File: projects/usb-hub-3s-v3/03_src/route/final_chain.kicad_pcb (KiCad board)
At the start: 4 copper layers, 130 x 92 mm, 114 parts, among them J1 C98732, J2 C503996, J3 C503996, J4 C503996, J5 C5337088, Q1 C2760089, Q2 C404363, Q3 C404363, Q4 C404363, Q5 C404363, Q6 C2760089, Q7 C78284, SW1 C2939728, U10 C7519, U11 C13755, U12 C7519, U2 C13755, U3 C130056, U4 C130056, U5 C130056, U6 C473910, U7 C473910, U8 C7519, U9 C7519

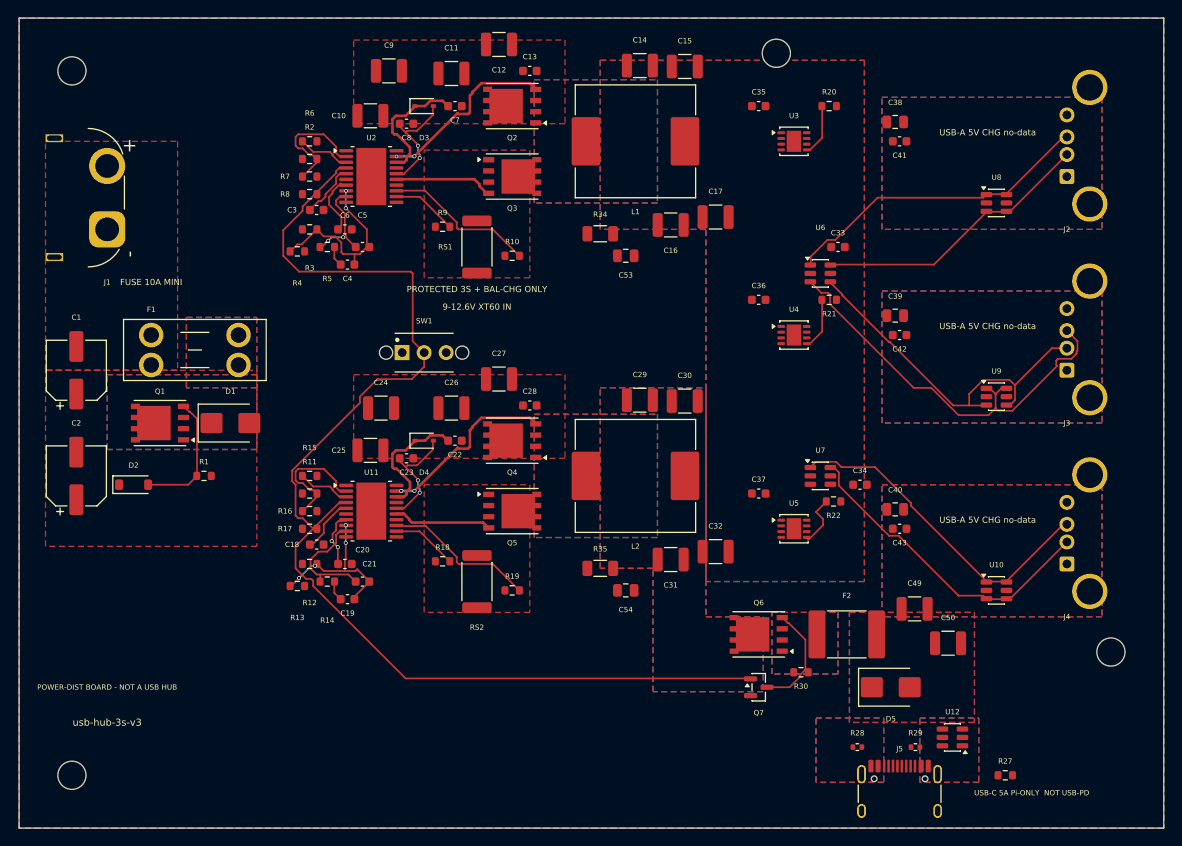
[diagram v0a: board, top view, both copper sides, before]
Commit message: usb-hub-3s-v3 v1.6: DRC 0/0/0 — the H3 screw-short is gone, and 11 CPL rows were off JLC's datum
v1.5 is DO-NOT-ORDER, and not for a reason any render could show. A new A-POS
gate measured every CPL row against JLC's convention — JLC positions a part
from the bounding box of its PAD CENTRES — and found the exporter had been
emitting fp.GetPosition(), the footprint ANCHOR. 11 of 108 rows were off-datum:
J1 4.6861mm, J2/J3/J4 3.7346mm, J5 1.4975mm, Q4/Q5/Q6 0.0625mm. Every external
connector, worst by nearly 5mm.

COPPER, all measured on FILLED zones before and after.

H3 was a short of the 6A rail to GND through a screw. MEASURED on sealed v1.5:
H3 (106,24) is a 1.600mm-radius NPTH whose F.Cu carries GND at 1.850mm AND 5VA
at 1.850mm, and whose B.Cu carries 5VA at 1.850 AND GND at 1.851. 0.250mm of
bare laminate and ~20um of mask, on both faces. EVERY M3 fastener bridges it —
not just a big washer, the smallest cap head (r 2.75) already does. v1.5's only
mitigation was a sentence in ORDER_README about nylon standoffs, which survives
exactly as long as the person who read it.

So v1.6 states a RULE instead of a note: within r <= 4.00mm of any mounting
hole, all outer copper is ONE net and that net is GND. Enforced three ways —
the 5VA pour is notched (5VA now stops at 4.500mm), the router's hole keepout
goes 3.0 -> 4.2mm so a signal wave cannot re-create it on a different net, and
the check is re-measured on the final filled board rather than assumed.

Also: H4's VBUSA3 4.152 -> 5.008mm (a DIN 9021 washer reached it); the In2 VIN
plane 1.850 -> 2.077mm on all four drills (0.250mm to a 12.6V plane, against a
+-0.13mm NPTH position tolerance, buried where no inspection will ever see it).
In1 GND is deliberately left at 1.850 — a grounded fastener touching GND is the
benign case and thinning the return plane costs more than it buys.

VBUS ampacity 0.5 -> 0.8mm. "Pour-fed" was true of the connector end and false
of the feed: each of VBUSA1/2/3 ran 13.554mm of 0.500mm B.Cu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
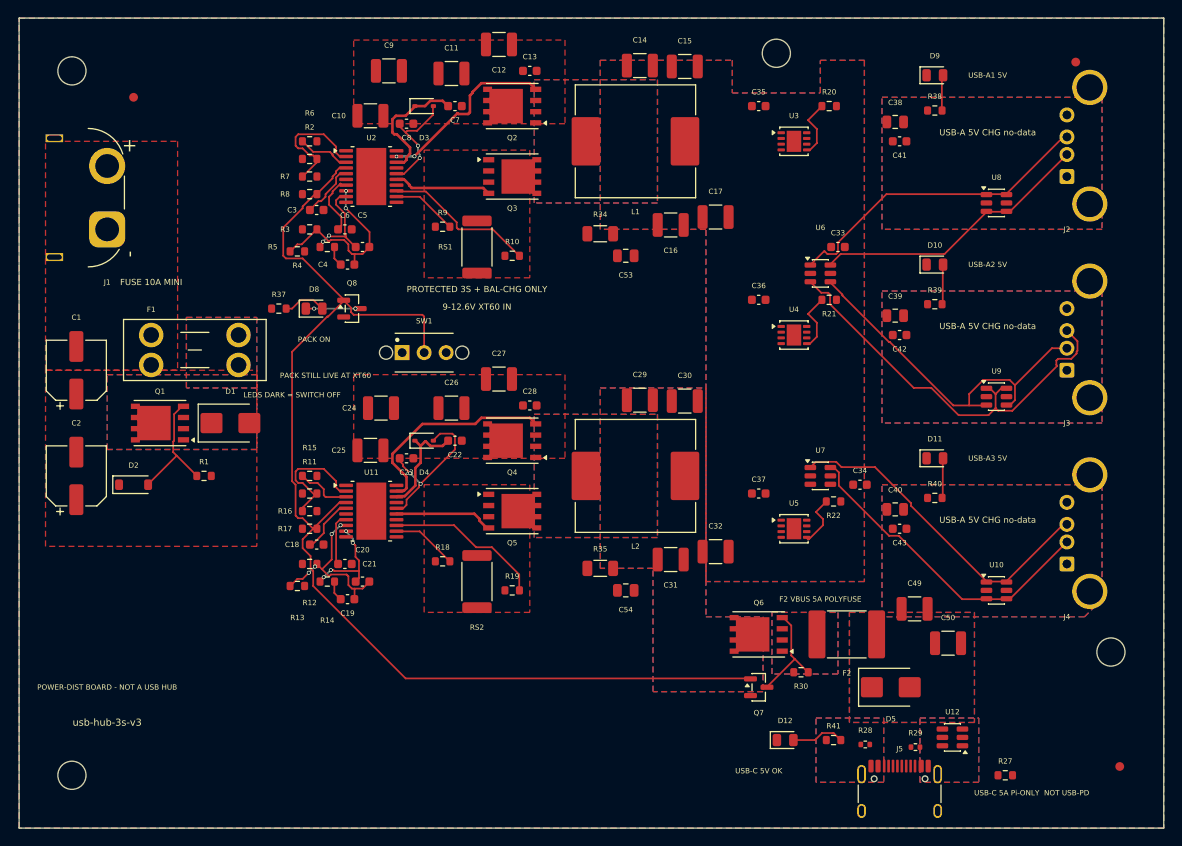
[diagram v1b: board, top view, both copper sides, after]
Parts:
- added D10: C2297, LED_SMD:LED_0805_2012Metric, F.Cu at (124.0, 48.0)
- added D11: C2297, LED_SMD:LED_0805_2012Metric, F.Cu at (124.0, 70.0)
- added D12: C2297, LED_SMD:LED_0805_2012Metric, F.Cu at (107.0, 102.0)
- added D8: C2296, LED_SMD:LED_0805_2012Metric, F.Cu at (53.5, 53.0)
- added D9: C2297, LED_SMD:LED_0805_2012Metric, F.Cu at (124.0, 26.5)
- added FID1: Fiducial_1mm_Mask2mm, Fiducial:Fiducial_1mm_Mask2mm, F.Cu at (33.0, 29.0)
- added FID2: Fiducial_1mm_Mask2mm, Fiducial:Fiducial_1mm_Mask2mm, F.Cu at (140.0, 25.0)
- added FID3: Fiducial_1mm_Mask2mm, Fiducial:Fiducial_1mm_Mask2mm, F.Cu at (145.0, 105.0)
- added Q8: C78284, Package_TO_SOT_SMD:SOT-23, F.Cu at (57.8, 53.0)
- added R37: 6.98kΩ, Resistor_SMD:R_0603_1608Metric, F.Cu at (49.5, 53.0)
- added R38: 6.98kΩ, Resistor_SMD:R_0603_1608Metric, F.Cu at (124.0, 30.5)
- added R39: 6.98kΩ, Resistor_SMD:R_0603_1608Metric, F.Cu at (124.0, 52.5)
- added R40: 6.98kΩ, Resistor_SMD:R_0603_1608Metric, F.Cu at (124.0, 74.5)
- added R41: 6.98kΩ, Resistor_SMD:R_0603_1608Metric, F.Cu at (112.5, 102.0)
- D5: value C140903 -> C113976
- moved R28 0.95 mm to (116.1, 102.5)
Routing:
- net LEDPKK: track 0.00 -> 6.17 mm, vias 0 -> 2
- net LEDVC: track 0.00 -> 6.13 mm
- net VCC_C: track 13.1 -> 18.3 mm
- net LEDPK: track 0.00 -> 4.99 mm
- net LEDVA3: track 0.00 -> 4.60 mm
- net LEDVA2: track 0.00 -> 4.60 mm
- net LEDVA1: track 0.00 -> 4.10 mm
- net HO_C: track 20.9 -> 24.2 mm, vias 2 -> 0
- net ENKILL: track 136.3 -> 133.5 mm
- net BOOT_C: track 14.5 -> 12.1 mm
- net COMP_C: track 13.5 -> 11.5 mm, vias 0 -> 4
- net FB_C: track 19.1 -> 20.1 mm
- net ILIM2: track 6.06 -> 6.89 mm
- net ILIM1: track 6.06 -> 6.89 mm
- net QG: track 12.9 -> 12.1 mm
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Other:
- board text added: "D10"
- board text added: "D11"
- board text added: "D12"
- board text added: "D8"
- board text added: "D9"
- board text added: "F2 VBUS 5A POLYFUSE"
- board text added: "FID1"
- board text added: "FID2"
- board text added: "FID3"
- board text added: "LEDS DARK = SWITCH OFF"
- board text added: "PACK ON"
- board text added: "PACK STILL LIVE AT XT60"
- board text added: "Q8"
- board text added: "R37"
- board text added: "R38"
- board text added: "R39"
- board text added: "R40"
- board text added: "R41"
- board text added: "USB-A1 5V"
- board text added: "USB-A2 5V"
- board text added: "USB-A3 5V"
- board text added: "USB-C 5V OK"

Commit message: usb-hub-3s-v3 v1.6: the load is a Pi 4, not a Pi 5 — the margin was never 15mV
Every power document on this board rested on one sentence, recorded at
commission as a "user + web-confirmed finding": that the Pi can be told to skip
PD negotiation and assume a 5A supply via `PSU_MAX_CURRENT=5000`.

THAT IS A RASPBERRY PI 5 BOOTLOADER-EEPROM FEATURE. The user has confirmed the
load is a Pi 4, which has no such setting and no equivalent.

The conclusion it justified — no PD source controller — survives. The reasoning
does not, and the difference is not cosmetic. A Pi 5 IS a PD sink; the old story
was "talk it out of negotiating", a deliberate departure from the normal
interface. A Pi 4 does not negotiate PD for its power input AT ALL: its USB-C
input is a plain 5V sink with CC pull-downs, officially 5V/3A (15W). There is no
profile to request and no override to set. A plain regulated rail is not a
workaround for a Pi 4 — it is the only interface it has.

An ADR whose stated reason is false is worse than no ADR, because it looks
decided. This fleet proved that twice today (cooksense's LMV393 "rail-to-rail"
claim, and this). So the digit is not swapped: ADR-0001 is marked
`superseded-by: 0004` (REASONING ONLY, its decision stands), ADR-0004 makes the
correct argument, and BRIEF.md keeps the old paragraph STRUCK rather than
deleted so the record of what was believed survives. T1 is rewritten (the
tension was never real), T3 is VOID (nothing for the user to forget), T4 is
added. `PSU_MAX_CURRENT` is purged from every live document — tsx header,
ARCHITECTURE, DETAIL_DESIGN, power_tree — and left only in the historical
reviews and the struck BRIEF text.

THE MARGIN IMPROVES 16.5x. Same hardware, same 97 mOhm budget, same 1.2
derating, same 5.227V worst-case rail, same 4.63V threshold. Only the load
changed, because we now know what it is:

    Pi 5 premise @ 5A: 582.0 mV drop -> 4.645 V ->  +15.0 mV slack
    Pi 4 actual  @ 3A: 349.2 mV drop -> 4.878 V -> +247.8 mV slack

E-MA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
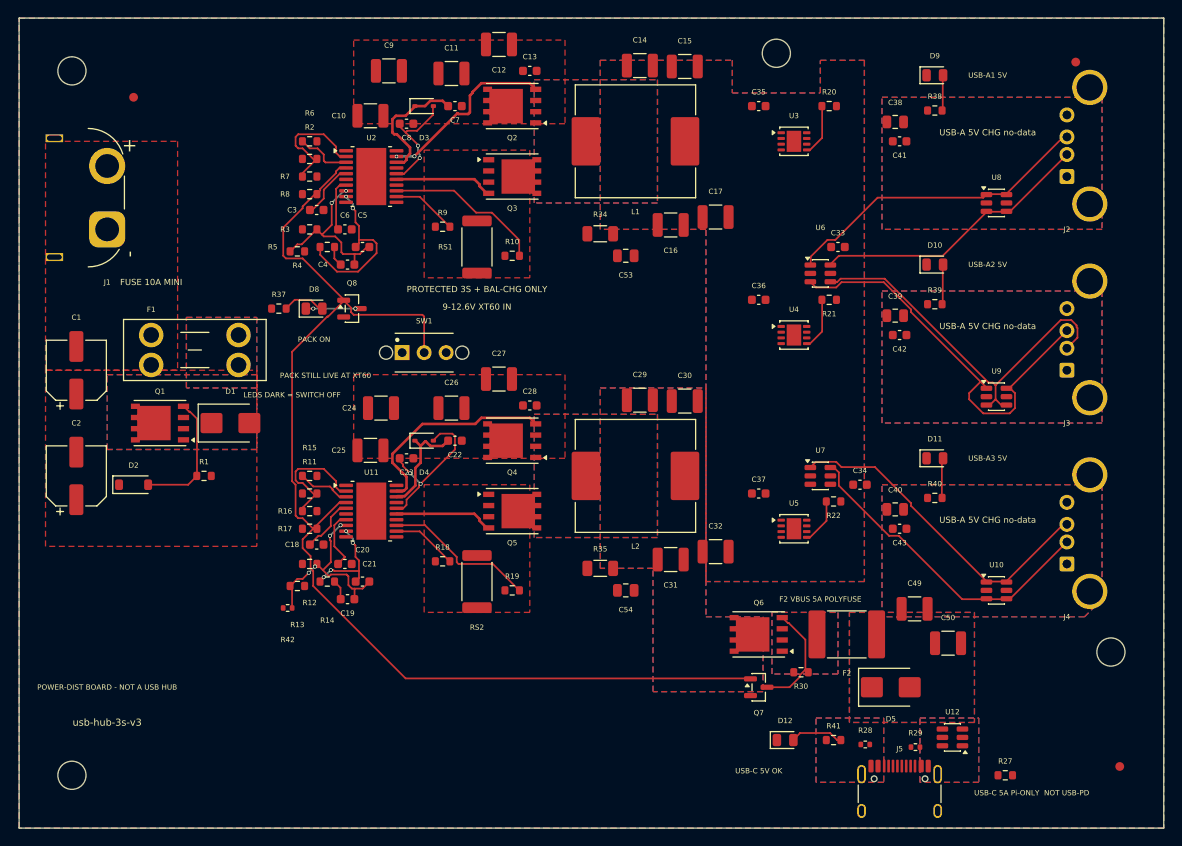
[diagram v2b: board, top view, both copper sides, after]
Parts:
- added R42: 160kΩ, Resistor_SMD:R_0402_1005Metric, F.Cu at (50.5, 87.0)
- Q1, Q2, Q3, Q4, Q5, Q6: footprint Package_SO:PowerPAK_SO-8_Single -> usb_hub_3s:PowerPAK_SO-8_Single_Paste65
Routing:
- net COMP_A: track 11.3 -> 18.8 mm
- net FB_C: track 20.1 -> 22.8 mm
- net DM_A2: track 41.8 -> 44.2 mm
- net DP_A2: track 48.4 -> 46.6 mm
- net SS_A: track 7.24 -> 6.02 mm
- net FB_A: track 20.9 -> 19.7 mm
- net ILIM3: track 6.25 -> 5.37 mm
- net SS_C: track 6.02 -> 6.85 mm
- net ILIM2: track 6.89 -> 6.06 mm
- net ILIM1: track 6.89 -> 6.06 mm
- net QG: track 12.1 -> 12.9 mm
- net CSGF_C: track 18.1 -> 17.5 mm
- net CSGF_A: track 17.5 -> 18.1 mm
- net ENKILL: track 133.5 -> 133.0 mm
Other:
- board text added: "R42"
